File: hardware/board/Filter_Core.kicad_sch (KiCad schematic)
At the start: 53 parts

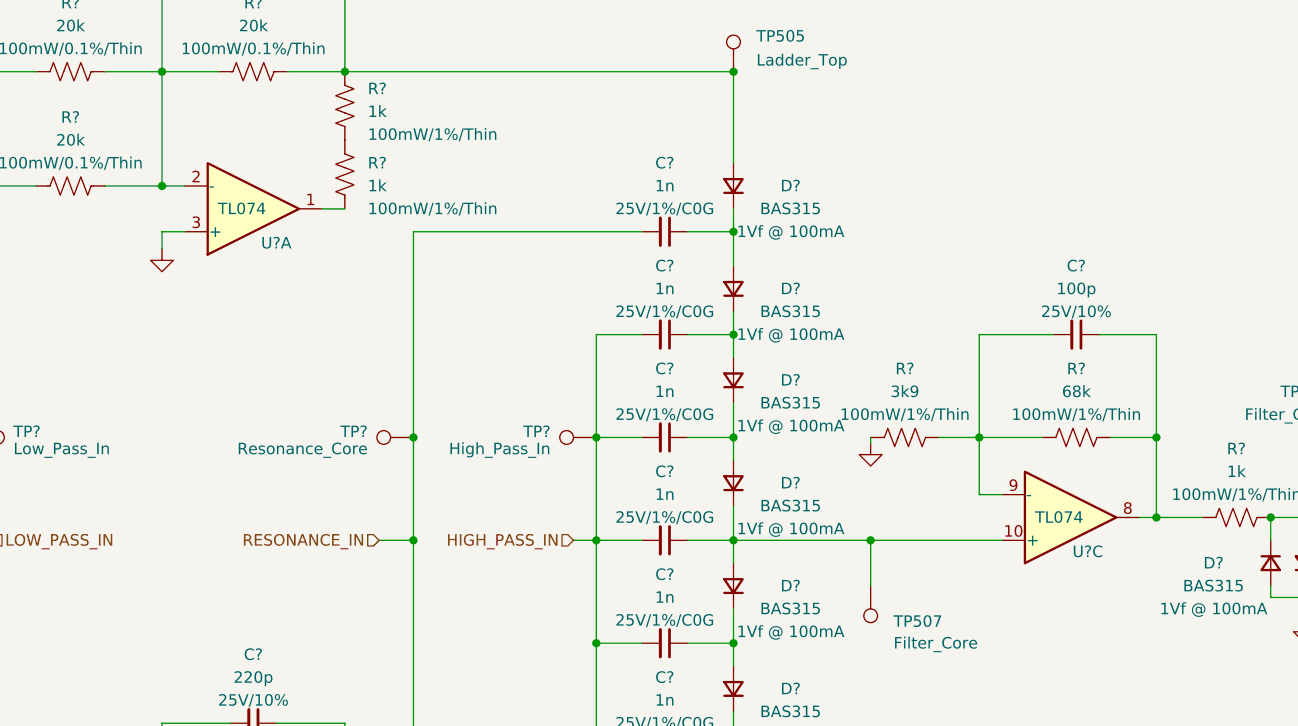
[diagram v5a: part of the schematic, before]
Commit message: First Draft of layout V2 (All components facing the same way)
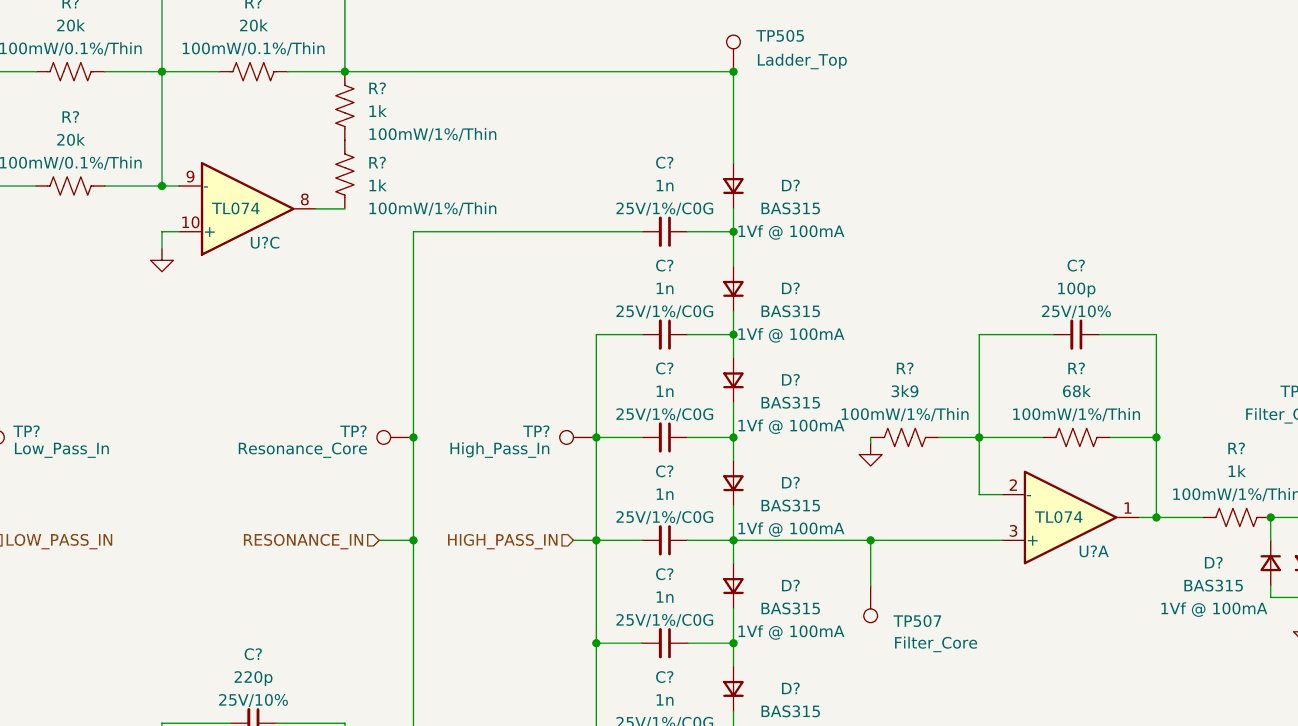
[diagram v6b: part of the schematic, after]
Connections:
- net GND: now also U?.10 (+); no longer U?.3 (+)
- net at C?.1, R?.1, R?.2: now also U?.1; no longer U?.8
- net at C?.2, R?.1, R?.1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: now also U?.9 (-); no longer U?.2 (-)
- net at C?.1, D?.1 (K), D?.2 (A)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: now also U?.3 (+); no longer U?.10 (+)
- net at R?.2: now also U?.8; no longer U?.1
- net at C?.2, R?.1, R?.2: now also U?.2 (-); no longer U?.9 (-)
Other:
- moved on the sheet: U?A, U?C
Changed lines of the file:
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@@
   (junction (at 189.23 66.04) (diameter 0) (color 0 0 0 0)
   )
+  (junction (at 204.47 88.9) (diameter 0) (color 0 0 0 0)
+  )
   (junction (at 146.05 132.08) (diameter 0) (color 0 0 0 0)
   )
@@
   (junction (at 252.73 95.25) (diameter 0) (color 0 0 0 0)
   )
+  (junction (at 125.73 49.53) (diameter 0) (color 0 0 0 0)
+  )
   (junction (at 189.23 132.08) (diameter 0) (color 0 0 0 0)
   )
@@
   (junction (at 189.23 54.61) (diameter 0) (color 0 0 0 0)
   )
-  (junction (at 204.47 88.9) (diameter 0) (color 0 0 0 0)
-  )
   (junction (at 189.23 36.83) (diameter 0) (color 0 0 0 0)
   )
@@
   (junction (at 90.17 134.62) (diameter 0) (color 0 0 0 0)
   )
+  (junction (at 236.22 86.36) (diameter 0) (color 0 0 0 0)
+  )
   (junction (at 125.73 134.62) (diameter 0) (color 0 0 0 0)
   )
@@
   (junction (at 189.23 77.47) (diameter 0) (color 0 0 0 0)
   )
-  (junction (at 236.22 86.36) (diameter 0) (color 0 0 0 0)
-  )
   (junction (at 104.14 88.9) (diameter 0) (color 0 0 0 0)
   )
@@
   (junction (at 173.99 77.47) (diameter 0) (color 0 0 0 0)
   )
-  (junction (at 125.73 49.53) (diameter 0) (color 0 0 0 0)
-  )
   (junction (at 125.73 36.83) (diameter 0) (color 0 0 0 0)
   )
@@
     (stroke (width 0) (type default))
   )
-  (wire (pts (xy 125.73 54.61) (xy 128.27 54.61))
+  (wire (pts (xy 216.535 83.82) (xy 219.075 83.82))
     (stroke (width 0) (type default))
   )
@@
     (stroke (width 0) (type default))
   )
-  (wire (pts (xy 125.73 49.53) (xy 128.27 49.53))
-    (stroke (width 0) (type default))
-  )
   (wire (pts (xy 125.73 36.83) (xy 132.08 36.83))
     (stroke (width 0) (type default))
@@
     (stroke (width 0) (type default))
   )
+  (wire (pts (xy 125.73 49.53) (xy 127.635 49.53))
+    (stroke (width 0) (type default))
+  )
   (wire (pts (xy 125.73 134.62) (xy 128.27 134.62))
     (stroke (width 0) (type default))
@@
     (stroke (width 0) (type default))
   )
-  (wire (pts (xy 216.535 83.82) (xy 219.075 83.82))
-    (stroke (width 0) (type default))
-  )
   (wire (pts (xy 90.17 134.62) (xy 90.17 147.32))
     (stroke (width 0) (type default))
@@
     (stroke (width 0) (type default))
   )
+  (wire (pts (xy 234.315 86.36) (xy 236.22 86.36))
+    (stroke (width 0) (type default))
+  )
   (wire (pts (xy 252.73 86.36) (xy 252.73 88.9))
     (stroke (width 0) (type default))
@@
     (stroke (width 0) (type default))
   )
+  (wire (pts (xy 142.875 52.07) (xy 146.05 52.07))
+    (stroke (width 0) (type default))
+  )
   (wire (pts (xy 153.67 77.47) (xy 153.67 88.9))
     (stroke (width 0) (type default))
@@
     (stroke (width 0) (type default))
   )
+  (wire (pts (xy 125.73 54.61) (xy 127.635 54.61))
+    (stroke (width 0) (type default))
+  )
+  (wire (pts (xy 125.73 56.515) (xy 125.73 54.61))
+    (stroke (width 0) (type default))
+  )
+  (wire (pts (xy 216.535 77.47) (xy 223.52 77.47))
+    (stroke (width 0) (type default))
+  )
+  (wire (pts (xy 77.47 86.36) (xy 81.28 86.36))
+    (stroke (width 0) (type default))
+  )
+  (wire (pts (xy 139.7 120.65) (xy 146.05 120.65))
+    (stroke (width 0) (type default))
+  )
+  (wire (pts (xy 189.23 88.9) (xy 204.47 88.9))
+    (stroke (width 0) (type default))
+  )
+  (wire (pts (xy 248.92 86.36) (xy 248.92 88.9))
+    (stroke (width 0) (type default))
+  )
+  (wire (pts (xy 104.14 49.53) (xy 111.76 49.53))
+    (stroke (width 0) (type default))
+  )
+  (wire (pts (xy 125.73 134.62) (xy 125.73 138.43))
+    (stroke (width 0) (type default))
+  )
+  (wire (pts (xy 189.23 63.5) (xy 189.23 66.04))
+    (stroke (width 0) (type default))
+  )
+  (wire (pts (xy 133.35 25.4) (xy 125.73 25.4))
+    (stroke (width 0) (type default))
+  )
   (wire (pts (xy 204.47 88.9) (xy 219.075 88.9))
     (stroke (width 0) (type default))
   )
-  (wire (pts (xy 125.73 56.515) (xy 125.73 54.61))
-    (stroke (width 0) (type default))
-  )
-  (wire (pts (xy 216.535 77.47) (xy 223.52 77.47))
-    (stroke (width 0) (type default))
-  )
-  (wire (pts (xy 77.47 86.36) (xy 81.28 86.36))
-    (stroke (width 0) (type default))
-  )
-  (wire (pts (xy 139.7 120.65) (xy 146.05 120.65))
-    (stroke (width 0) (type default))
-  )
-  (wire (pts (xy 189.23 88.9) (xy 204.47 88.9))
-    (stroke (width 0) (type default))
-  )
-  (wire (pts (xy 248.92 86.36) (xy 248.92 88.9))
-    (stroke (width 0) (type default))
-  )
-  (wire (pts (xy 104.14 49.53) (xy 111.76 49.53))
-    (stroke (width 0) (type default))
-  )
-  (wire (pts (xy 125.73 134.62) (xy 125.73 138.43))
-    (stroke (width 0) (type default))
-  )
-  (wire (pts (xy 189.23 63.5) (xy 189.23 66.04))
-    (stroke (width 0) (type default))
-  )
-  (wire (pts (xy 133.35 25.4) (xy 125.73 25.4))
-    (stroke (width 0) (type default))
-  )
   (wire (pts (xy 184.15 88.9) (xy 189.23 88.9))
     (stroke (width 0) (type default))
@@
     (stroke (width 0) (type default))
   )
-  (wire (pts (xy 234.315 86.36) (xy 236.22 86.36))
-    (stroke (width 0) (type default))
-  )
   (wire (pts (xy 189.23 66.04) (xy 189.23 68.58))
     (stroke (width 0) (type default))
@@
   )
   (wire (pts (xy 146.05 36.83) (xy 146.05 25.4))
-    (stroke (width 0) (type default))
-  )
-  (wire (pts (xy 143.51 52.07) (xy 146.05 52.07))
     (stroke (width 0) (type default))
   )
@@
     )
   )
-  (symbol (lib_id "winterbloom:TL074") (at 226.695 86.36 0) (mirror x) (unit 3)
+  (symbol (lib_id "winterbloom:TL074") (at 135.255 52.07 0) (mirror x) (unit 3)
     (in_bom yes) (on_board yes) (dnp no)
-    (property "Reference" "U?" (at 228.6 90.17 0)
-      (effects (font (size 1.27 1.27)))
-    )
-    (property "Value" "TL074" (at 225.425 86.36 0)
-      (effects (font (size 1.27 1.27)))
-    )
-    (property "Footprint" "Package_SO:TSSOP-14_4.4x5mm_P0.65mm" (at 226.695 96.52 0)
-      (effects (font (size 1.27 1.27)) hide)
-    )
-    (property "Datasheet" "https://www.ti.com/lit/ds/symlink/tl071.pdf" (at 227.965 91.44 0)
-      (effects (font (size 1.27 1.27)) hide)
-    )
-    (property "MPN" "TL074CPW" (at 226.695 93.98 0)
+    (property "Reference" "U?" (at 137.16 55.88 0)
+      (effects (font (size 1.27 1.27)))
+    )
+    (property "Value" "TL074" (at 133.985 52.07 0)
+      (effects (font (size 1.27 1.27)))
+    )
+    (property "Footprint" "Package_SO:TSSOP-14_4.4x5mm_P0.65mm" (at 135.255 62.23 0)
+      (effects (font (size 1.27 1.27)) hide)
+    )
+    (property "Datasheet" "https://www.ti.com/lit/ds/symlink/tl071.pdf" (at 136.525 57.15 0)
+      (effects (font (size 1.27 1.27)) hide)
+    )
+    (property "MPN" "TL074CPW" (at 135.255 59.69 0)
       (effects (font (size 1.27 1.27)) hide)
     )
@@
     )
   )
-  (symbol (lib_id "winterbloom:TL074") (at 135.89 52.07 0) (mirror x) (unit 1)
+  (symbol (lib_id "winterbloom:TL074") (at 226.695 86.36 0) (mirror x) (unit 1)
     (in_bom yes) (on_board yes) (dnp no)
-    (property "Reference" "U?" (at 138.43 55.88 0)
-      (effects (font (size 1.27 1.27)))
-    )
-    (property "Value" "TL074" (at 134.62 52.07 0)
-      (effects (font (size 1.27 1.27)))
-    )
-    (property "Footprint" "Package_SO:TSSOP-14_4.4x5mm_P0.65mm" (at 135.89 62.23 0)
-      (effects (font (size 1.27 1.27)) hide)
-    )
-    (property "Datasheet" "https://www.ti.com/lit/ds/symlink/tl071.pdf" (at 137.16 57.15 0)
-      (effects (font (size 1.27 1.27)) hide)
-    )
-    (property "MPN" "TL074CPW" (at 135.89 59.69 0)
-      (effects (font (size 1.27 1.27)) hide)
-    )
+    (property "Reference" "U?" (at 229.235 90.17 0)
+      (effects (font (size 1.27 1.27)))
+    )
+    (property "Value" "TL074" (at 225.425 86.36 0)
+      (effects (font (size 1.27 1.27)))
+    )
+    (property "Footprint" "Package_SO:TSSOP-14_4.4x5mm_P0.65mm" (at 226.695 96.52 0)
+      (effects (font (size 1.27 1.27)) hide)
+    )
+    (property "Datasheet" "https://www.ti.com/lit/ds/symlink/tl071.pdf" (at 227.965 91.44 0)
+      (effects (font (size 1.27 1.27)) hide)
+    )
+    (property "MPN" "TL074CPW" (at 226.695 93.98 0)
+      (effects (font (size 1.27 1.27)) hide)
+    )

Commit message: Rough Draft of Routing Complete. Ugly but Passes DRC
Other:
- note added: "4 Pole Diode Ladder Filter Core Low Pass and High Pass Input Amplitude Range: ±50mV nominal max volume Resonance Input Self Oscillation Threshold: ~200mV Cutoff Input Limits: Low: 2.5v = ~3hz High: -7.9v = ~100khz Output Nominal Amplitude: ±300mV Output Max Amplitude: ±450mV Ladder Op Amp Cutoff Frequency: ~20kHz"
- note removed: "4 Pole Diode Ladder Filter Core Low Pass and High Pass Input Amplitude Range: ±50mV nominal max volume Resonance Input Self Oscillation Threshold: ~200mV Cutoff Input Limits: Low: 2.5v = ~3hz High: -7.9v = ~100khz Output Nominal Amplitude: ±300mV Output Max Amplitude: ±450mV Op Amp Compensation Cutoff Frequency: ~20kHz"
- note removed: "High and low cutoff limiters are slightly voodoo majik, I got these values playing with the sim and changing things on my prototypes. Since they are part of a network of resistors the voltage changes with the cutoff frequency."
- moved on the sheet: C?, D?, R?, TP507, TP508, U?A

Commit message: Final touches before being ready for ordering
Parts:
- C? (x2): value 220p -> 100p
- R?: Rating 100mW/0.1%/Thin -> 100mW/1%/Thin
- R?: value 1k -> 1k8
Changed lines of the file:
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@@
       (effects (font (size 1.27 1.27)))
     )
-    (property "Value" "220p" (at 135.8836 20.32 90)
+    (property "Value" "100p" (at 135.8836 20.32 90)
       (effects (font (size 1.27 1.27)))
     )
@@
       (effects (font (size 1.27 1.27)))
     )
-    (property "Value" "220p" (at 135.8836 104.14 90)
+    (property "Value" "100p" (at 135.8836 104.14 90)
       (effects (font (size 1.27 1.27)))
     )
@@
       (effects (font (size 1.27 1.27)) hide)
     )
-    (property "Rating" "100mW/0.1%/Thin" (at 79.375 156.21 90)
+    (property "Rating" "100mW/1%/Thin" (at 79.375 156.21 90)
       (effects (font (size 1.27 1.27)))
     )
@@
       (effects (font (size 1.27 1.27)))
     )
-    (property "Value" "1k" (at 35.56 123.19 90)
-      (effects (font (size 1.27 1.27)))
-    )
+    (property "Value" "1k8" (at 35.56 123.19 90)
+      (effects (font (size 1.27 1.27)))
+    )
